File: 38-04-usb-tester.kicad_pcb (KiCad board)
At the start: 2 copper layers, 125.9 x 97.8 mm, 68 parts, among them J1 Conn_1x05, J2 USB_C_12401832E402A, J3 USB_C_12401832E402A, J4 USB_Micro-B_KH-MICRO5P-JN, J5 USB_Mini-B_U-M-M5DD-W-1, J6 USB3_A_HC-USB3.0-L168-WP, SW1 SW_SPDT, SW2 ZX-1.27BM-4PSMD, U1 STM32C031K6Tx

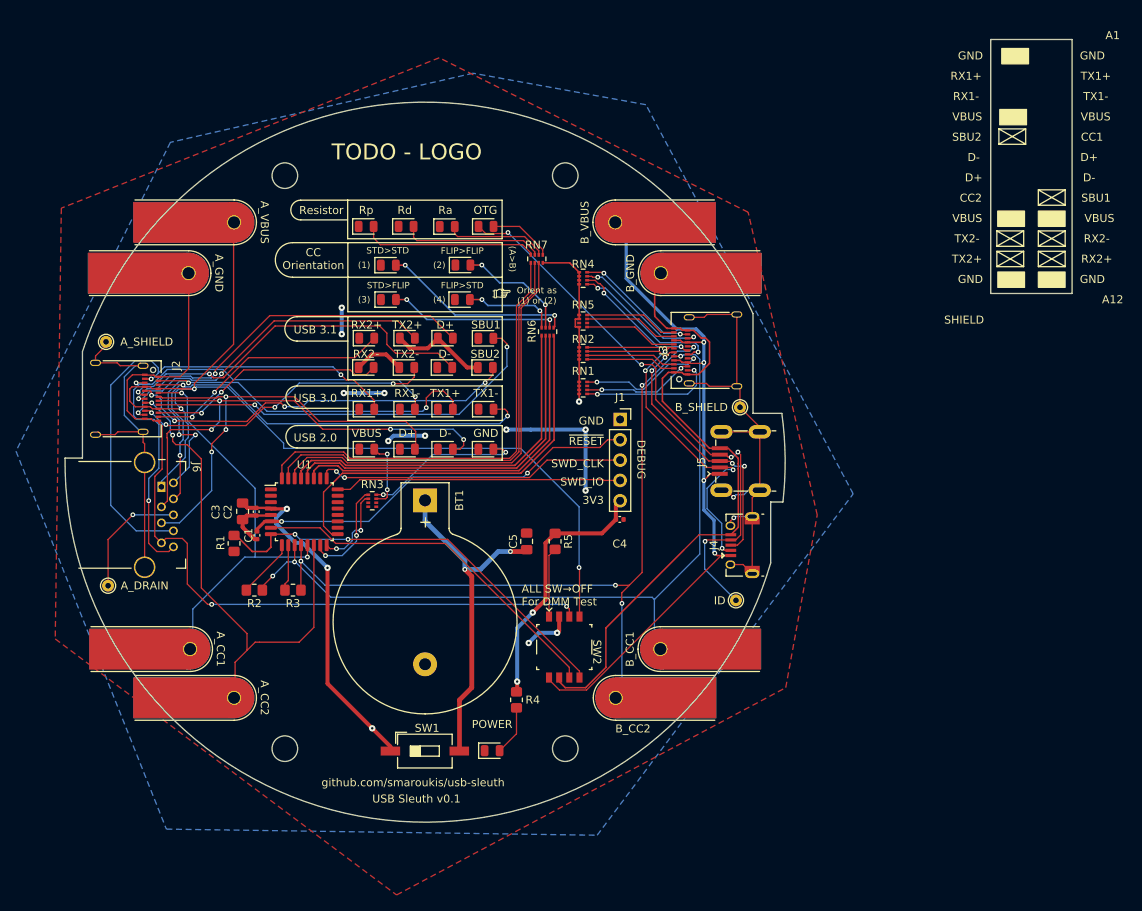
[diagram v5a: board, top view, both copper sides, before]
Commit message: moved usb footprints from  board edge
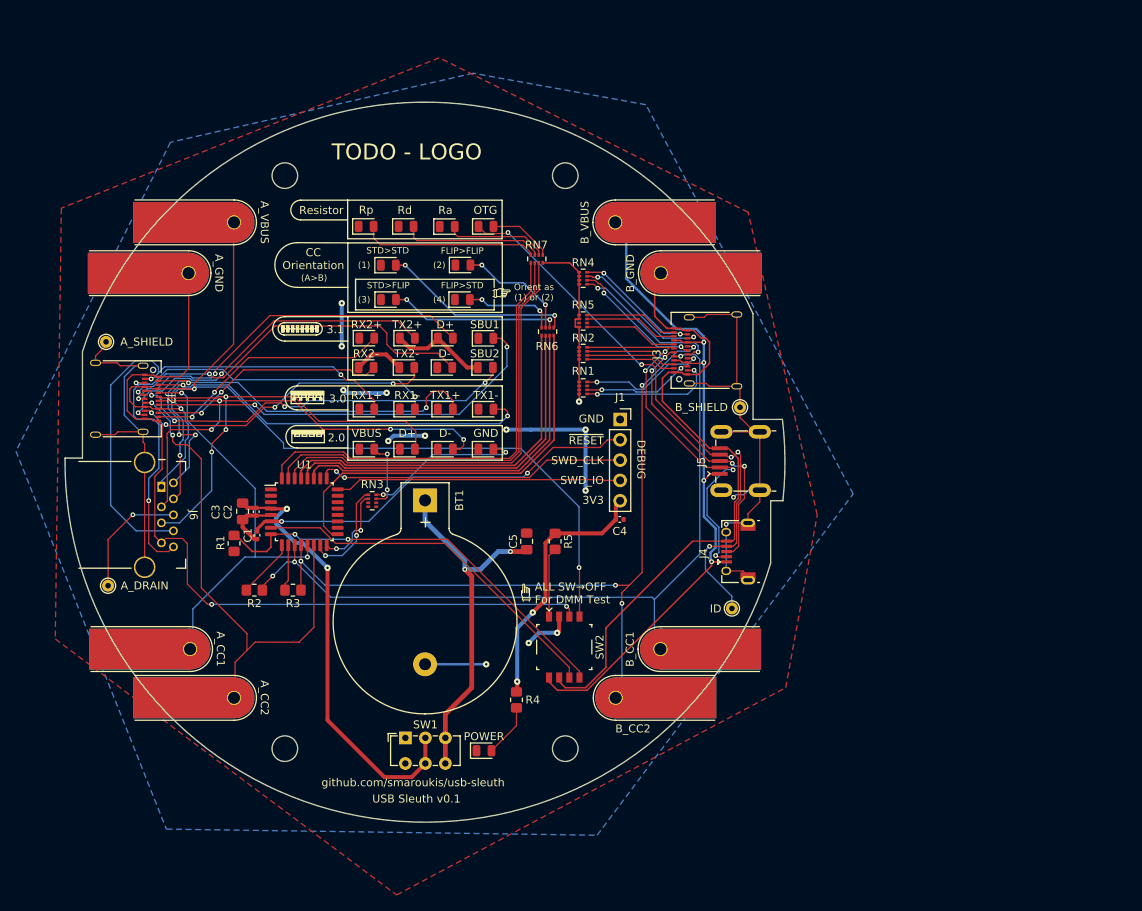
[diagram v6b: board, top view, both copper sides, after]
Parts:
- SW1: value SW_SPDT -> SW_DPDT_x2; footprint Button_Switch_SMD:SW_DIP_SPSTx01_Slide_6.7x4.1mm_W8.61mm_P2.54mm_LowProfile -> Button_Switch_THT:SW_E-Switch_EG1271_SPDT
- moved SW1 2.94 mm to (152.5, 145.0)
- moved H11 1.14 mm to (193.3, 128.8)
- moved D1 1.02 mm to (162.3, 146.6)
- moved J4 0.96 mm to (195.3, 121.7)
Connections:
- SW1 pad 1: VCC -> unconnected-(SW1A-A-Pad1)
- SW1 pad 2: Net-(BT1-+) -> VCC
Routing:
- net VCC: track 98.1 -> 110.1 mm, vias 6 -> 5
- net GND: track 63.3 -> 73.5 mm, vias 11 -> 12
- net Net-(BT1-+): track 43.2 -> 45.4 mm
- net /B_D1-: track 47.7 -> 49.4 mm
- net /B_D1+: track 44.1 -> 45.4 mm
- net /A_SHIELD: track 44.8 -> 43.8 mm
- net /B_GND_A1: track 82.6 -> 83.2 mm
- net /B_VBUS_A4: track 90.1 -> 89.6 mm
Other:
- board size 125.9 x 97.8 mm -> 90 x 90 mm
- board text added: "2.0"
- board text added: "3.0"
- board text added: "3.1"
- board text added: "JLPCB Constraints (2 Layer) - Min Trace Width = 0.127 - Min Trace Spacing = 0.127 - Text Line Width >= 0.153mm (6mil) - Text Height > 1mm - Pad to Silkscreen >= 0.15mm - Trace to Board Edge >= 0.3mm - PTH to Track >= 0.33m - NPTH to Track >= 0.254mm - Pad to Track >= 0.2mm *: Not avail. in editor settings"
- board text removed: "A1"
- board text removed: "A12"
- board text removed: "CC1"
- board text removed: "CC2"
- board text removed: "SHIELD"
- board text removed: "USB 2.0"
- board text removed: "USB 3.0"
- board text removed: "USB 3.1"

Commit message: renamed user symbol file
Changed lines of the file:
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@@
     (solder_mask_min_width 0.12)
     (aux_axis_origin 10.16 10.16)
-    (grid_origin 135.636 116.332)
+    (grid_origin 76.2 150.4188)
     (pcbplotparams
       (layerselection 0x00010fc_ffffffff)
@@
     (descr "E-Switch sub miniature slide switch, EG series, SPDT, https://www.e-switch.com/wp-content/uploads/2022/06/EG.pdf")
     (tags "switch SPDT")
+    (property "JLPCB_MPN" "DNP")
+    (property "JLPCB_Mfg" "DNP")
+    (property "JLPCB_Part_No" "DNP")
+    (property "JLPCB_Price" "DNP")
     (property "JLPCB_URL" "")
     (property "Sheetfile" "38-04-usb-tester.kicad_sch")
@@
       (net 27 "unconnected-(U1-PB9-Pad1)") (pinfunction "PB9") (pintype "bidirectional"))
     (pad "2" smd roundrect (at -4.175 -2) (size 1.5 0.5) (layers "F.Cu" "F.Paste" "F.Mask") (roundrect_rratio 0.25)
-      (net 28 "unconnected-(U1-PC14-Pad2)") (pinfunction "PC14") (pintype "bidirectional"))
+      (net 28 "unconnected-(U1-PC14-Pad2)") (pinfunction "PC14") (pintype "bidirectional+no_connect"))
     (pad "3" smd roundrect (at -4.175 -1.2) (size 1.5 0.5) (layers "F.Cu" "F.Paste" "F.Mask") (roundrect_rratio 0.25)
-      (net 29 "unconnected-(U1-PC15-Pad3)") (pinfunction "PC15") (pintype "bidirectional"))
+      (net 29 "unconnected-(U1-PC15-Pad3)") (pinfunction "PC15") (pintype "bidirectional+no_connect"))
     (pad "4" smd roundrect (at -4.175 -0.4) (size 1.5 0.5) (layers "F.Cu" "F.Paste" "F.Mask") (roundrect_rratio 0.25)
       (net 30 "VCC") (pinfunction "VDD") (pintype "power_in"))
@@
       (net 69 "/CC_aa") (pinfunction "PB2") (pintype "bidirectional"))
     (pad "18" smd roundrect (at 4.175 2) (size 1.5 0.5) (layers "F.Cu" "F.Paste" "F.Mask") (roundrect_rratio 0.25)
-      (net 43 "unconnected-(U1-PA8-Pad18)") (pinfunction "PA8") (pintype "bidirectional"))
+      (net 43 "unconnected-(U1-PA8-Pad18)") (pinfunction "PA8") (pintype "bidirectional+no_connect"))
     (pad "19" smd roundrect (at 4.175 1.2) (size 1.5 0.5) (layers "F.Cu" "F.Paste" "F.Mask") (roundrect_rratio 0.25)
-      (net 44 "unconnected-(U1-PA9{slash}NC-Pad19)") (pinfunction "PA9/NC") (pintype "bidirectional"))
+      (net 44 "unconnected-(U1-PA9{slash}NC-Pad19)") (pinfunction "PA9/NC") (pintype "bidirectional+no_connect"))
     (pad "20" smd roundrect (at 4.175 0.4) (size 1.5 0.5) (layers "F.Cu" "F.Paste" "F.Mask") (roundrect_rratio 0.25)
-      (net 45 "unconnected-(U1-PC6-Pad20)") (pinfunction "PC6") (pintype "bidirectional"))
+      (net 45 "unconnected-(U1-PC6-Pad20)") (pinfunction "PC6") (pintype "bidirectional+no_connect"))
     (pad "21" smd roundrect (at 4.175 -0.4) (size 1.5 0.5) (layers "F.Cu" "F.Paste" "F.Mask") (roundrect_rratio 0.25)
-      (net 46 "unconnected-(U1-PA10{slash}NC-Pad21)") (pinfunction "PA10/NC") (pintype "bidirectional"))
+      (net 46 "unconnected-(U1-PA10{slash}NC-Pad21)") (pinfunction "PA10/NC") (pintype "bidirectional+no_connect"))
     (pad "22" smd roundrect (at 4.175 -1.2) (size 1.5 0.5) (layers "F.Cu" "F.Paste" "F.Mask") (roundrect_rratio 0.25)
-      (net 47 "unconnected-(U1-PA11{slash}PA9-Pad22)") (pinfunction "PA11/PA9") (pintype "bidirectional"))
+      (net 47 "unconnected-(U1-PA11{slash}PA9-Pad22)") (pinfunction "PA11/PA9") (pintype "bidirectional+no_connect"))
     (pad "23" smd roundrect (at 4.175 -2) (size 1.5 0.5) (layers "F.Cu" "F.Paste" "F.Mask") (roundrect_rratio 0.25)
-      (net 48 "unconnected-(U1-PA12{slash}PA10-Pad23)") (pinfunction "PA12/PA10") (pintype "bidirectional"))
+      (net 48 "unconnected-(U1-PA12{slash}PA10-Pad23)") (pinfunction "PA12/PA10") (pintype "bidirectional+no_connect"))
     (pad "24" smd roundrect (at 4.175 -2.8) (size 1.5 0.5) (layers "F.Cu" "F.Paste" "F.Mask") (roundrect_rratio 0.25)
       (net 49 "/SWDIO") (pinfunction "PA13") (pintype "bidirectional"))
@@
       (net 50 "/SWCLK_BOOT0") (pinfunction "PA14") (pintype "bidirectional"))
     (pad "26" smd roundrect (at 2 -4.175) (size 0.5 1.5) (layers "F.Cu" "F.Paste" "F.Mask") (roundrect_rratio 0.25)
-      (net 51 "unconnected-(U1-PA15-Pad26)") (pinfunction "PA15") (pintype "bidirectional"))
+      (net 51 "unconnected-(U1-PA15-Pad26)") (pinfunction "PA15") (pintype "bidirectional+no_connect"))
     (pad "27" smd roundrect (at 1.2 -4.175) (size 0.5 1.5) (layers "F.Cu" "F.Paste" "F.Mask") (roundrect_rratio 0.25)
       (net 70 "/CC_ab") (pinfunction "PB3") (pintype "bidirectional"))
@@
     (effects (font (size 1 1) (thickness 0.15)))
   )
-  (gr_text "TODO - LOGO" (at 143.256 72.898) (layer "F.SilkS")
+  (gr_text "TODO - LOGO" (at 143.764 57.9628) (layer "F.SilkS")
     (effects (font (size 2 2) (thickness 0.15)) (justify left bottom))
   )

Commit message: renamed libraries
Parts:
- H1, H10, H2, H3, H4, H5, H7, H9: footprint 01-UserLibary:Connector_Pad_Edge_Oval_5mm_Extended -> 01-UserFootprints:Connector_Pad_Edge_Oval_5mm_Extended
- J2, J3: footprint 01-UserLibary:USB_C_Receptacle_Amphenol_12401832E402A -> 01-UserFootprints:USB_C_Receptacle_Amphenol_12401832E402A
- J4: footprint 01-UserLibary:USB_Micro-B_Kinghelm-KH-MICRO5P-JN -> 01-UserFootprints:USB_Micro-B_Kinghelm-KH-MICRO5P-JN
- J5: footprint 01-UserLibary:USB_Mini-B_Korean-Hroparts_U-M-M5DD-W-1_SMD-5-4MP -> 01-UserFootprints:USB_Mini-B_Korean-Hroparts_U-M-M5DD-W-1_SMD-5-4MP
- J6: footprint 01-UserLibary:USB3_A_Hong-Cheng_HC-USB3.0-L168-WP_THT-9-2MP_P2.0mm -> 01-UserFootprints:USB3_A_Hong-Cheng_HC-USB3.0-L168-WP_THT-9-2MP_P2.0mm
- SW2: footprint 01-UserLibary:SW-DIP-4P_P1.27mm_SMD-2x4 -> 01-UserFootprints:SW-DIP-4P_P1.27mm_SMD-2x4
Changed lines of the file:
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@@
       (net 85 "/B_SHIELD") (pinfunction "1") (pintype "input"))
   )
-  (footprint "01-UserLibary:Connector_Pad_Edge_Oval_5mm_Extended" (layer "F.Cu")
+  (footprint "01-UserFootprints:Connector_Pad_Edge_Oval_5mm_Extended" (layer "F.Cu")
     (at 196.9 133.858 90)
     (property "Description" "B_CC1")
@@
     )
   )
-  (footprint "01-UserLibary:Connector_Pad_Edge_Oval_5mm_Extended" (layer "F.Cu")
+  (footprint "01-UserFootprints:Connector_Pad_Edge_Oval_5mm_Extended" (layer "F.Cu")
     (at 113.03 133.858 -90)
     (property "Description" "A_CC1")
@@
       ))
   )
-  (footprint "01-UserLibary:USB_C_Receptacle_Amphenol_12401832E402A" (layer "F.Cu")
+  (footprint "01-UserFootprints:USB_C_Receptacle_Amphenol_12401832E402A" (layer "F.Cu")
     (at 116.586 102.568 -90)
     (descr "USB TYPE C, RA RCPT PCB, SMT, https://jlcpcb.com/partdetail/AmphenolIcc-12401832E402A/C464604")
@@
     )
   )
-  (footprint "01-UserLibary:Connector_Pad_Edge_Oval_5mm_Extended" (layer "F.Cu")
+  (footprint "01-UserFootprints:Connector_Pad_Edge_Oval_5mm_Extended" (layer "F.Cu")
     (at 196.95 86.868 90)
     (property "Description" "B_GND")
@@
     )
   )
-  (footprint "01-UserLibary:USB_C_Receptacle_Amphenol_12401832E402A" (layer "F.Cu")
+  (footprint "01-UserFootprints:USB_C_Receptacle_Amphenol_12401832E402A" (layer "F.Cu")
     (at 191.07 96.52 90)
     (descr "USB TYPE C, RA RCPT PCB, SMT, https://jlcpcb.com/partdetail/AmphenolIcc-12401832E402A/C464604")
@@
     )
   )
-  (footprint "01-UserLibary:USB_Mini-B_Korean-Hroparts_U-M-M5DD-W-1_SMD-5-4MP" (layer "F.Cu")
+  (footprint "01-UserFootprints:USB_Mini-B_Korean-Hroparts_U-M-M5DD-W-1_SMD-5-4MP" (layer "F.Cu")
     (at 191.78 110.351 180)
     (property "Description" "USB-B-Mini")
@@
     )
   )
-  (footprint "01-UserLibary:USB_Micro-B_Kinghelm-KH-MICRO5P-JN" (layer "F.Cu")
+  (footprint "01-UserFootprints:USB_Micro-B_Kinghelm-KH-MICRO5P-JN" (layer "F.Cu")
     (at 195.304 121.666 90)
     (descr "Micro USB B Receptacel (https://jlcpcb.com/partdetail/Shenzhen_KinghelmElec-KH_MICRO5PJN/C962222)")
@@
     )
   )
-  (footprint "01-UserLibary:Connector_Pad_Edge_Oval_5mm_Extended" (layer "F.Cu")
+  (footprint "01-UserFootprints:Connector_Pad_Edge_Oval_5mm_Extended" (layer "F.Cu")
     (at 191.308 139.954 90)
     (property "Description" "B_CC2")
@@
     )
   )
-  (footprint "01-UserLibary:Connector_Pad_Edge_Oval_5mm_Extended" (layer "F.Cu")
+  (footprint "01-UserFootprints:Connector_Pad_Edge_Oval_5mm_Extended" (layer "F.Cu")
     (at 118.524 139.954 -90)
     (property "Description" "A_CC2")
@@
     )
   )
-  (footprint "01-UserLibary:Connector_Pad_Edge_Oval_5mm_Extended" (layer "F.Cu")
+  (footprint "01-UserFootprints:Connector_Pad_Edge_Oval_5mm_Extended" (layer "F.Cu")
     (at 112.836 86.868 -90)
     (property "Description" "A_GND")
@@
     )
   )
-  (footprint "01-UserLibary:Connector_Pad_Edge_Oval_5mm_Extended" (layer "F.Cu")
+  (footprint "01-UserFootprints:Connector_Pad_Edge_Oval_5mm_Extended" (layer "F.Cu")
     (at 118.524 80.518 -90)
     (property "Description" "A_VBUS")
@@
     )
   )
-  (footprint "01-UserLibary:SW-DIP-4P_P1.27mm_SMD-2x4" (layer "F.Cu")
+  (footprint "01-UserFootprints:SW-DIP-4P_P1.27mm_SMD-2x4" (layer "F.Cu")
     (at 172.339 133.604)
     (property "Description" "SW - Isolator")
@@
     (pad "" np_thru_hole circle locked (at 0 0) (size 3.2 3.2) (drill 3.2) (layers "F&B.Cu" "*.Mask"))
   )
-  (footprint "01-UserLibary:Connector_Pad_Edge_Oval_5mm_Extended" (layer "F.Cu")
+  (footprint "01-UserFootprints:Connector_Pad_Edge_Oval_5mm_Extended" (layer "F.Cu")
     (at 191.258 80.518 90)
     (property "Description" "B_VBUS")
@@
       (net 22 "/A_DRAIN") (pinfunction "1") (pintype "input"))
   )
-  (footprint "01-UserLibary:USB3_A_Hong-Cheng_HC-USB3.0-L168-WP_THT-9-2MP_P2.0mm" locked (layer "F.Cu")
+  (footprint "01-UserFootprints:USB3_A_Hong-Cheng_HC-USB3.0-L168-WP_THT-9-2MP_P2.0mm" locked (layer "F.Cu")
     (at 123.488 117.078 -90)
     (property "Description" "USB-A-3.0")
